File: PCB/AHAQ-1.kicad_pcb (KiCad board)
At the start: 4 copper layers, 50 x 50 mm, 62 parts, among them J1 USB_C_Receptacle_USB2.0_16P, J2 UART, J3 I2C_3, J4 SEN55, J5 I2C_1, J6 I2C_2, J7 I2C_4, J9 E-Paper, Q1 Si1308EDL, U1 ESP32-C6-MINI-1/U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

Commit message: Rename to AHQA-1, README
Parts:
- removed C30, C31: 100nF, Capacitor_SMD:C_0603_1608Metric
- removed J6: I2C_2, Connector_JST:JST_SH_BM04B-SRSS-TB_1x04-1MP_P1.00mm_Vertical
- removed J7: I2C_4, Connector_JST:JST_SH_BM04B-SRSS-TB_1x04-1MP_P1.00mm_Vertical
- J2: footprint Connector_JST:JST_SH_BM03B-SRSS-TB_1x03-1MP_P1.00mm_Vertical -> Connector_JST:JST_SH_SM03B-SRSS-TB_1x03-1MP_P1.00mm_Horizontal
- J3: value I2C_3 -> I2C_1; footprint Connector_JST:JST_SH_BM04B-SRSS-TB_1x04-1MP_P1.00mm_Vertical -> Connector_JST:JST_SH_SM04B-SRSS-TB_1x04-1MP_P1.00mm_Horizontal
- J4: renamed from J5; footprint Connector_JST:JST_SH_BM04B-SRSS-TB_1x04-1MP_P1.00mm_Vertical -> Connector_JST:JST_SH_SM04B-SRSS-TB_1x04-1MP_P1.00mm_Horizontal
- moved J3 12.2 mm to (91.5, 81.5)
- moved J4 8.83 mm to (91.5, 66.0)
- moved C29 5.30 mm to (89.2, 70.0)
- moved J2 1.10 mm to (89.5, 53.3)
- moved C28 1.00 mm to (89.2, 81.5)
- renumbered J4 to J5
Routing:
- net GND: track 167.9 -> 155.0 mm, vias 127 -> 124
- net UART_TX: track 30.6 -> 26.3 mm
- net UART_RX: track 28.9 -> 24.5 mm
- net +3V3_SEN: track 41.0 -> 38.5 mm, vias 9 -> 7
- net SDA: track 90.9 -> 90.2 mm

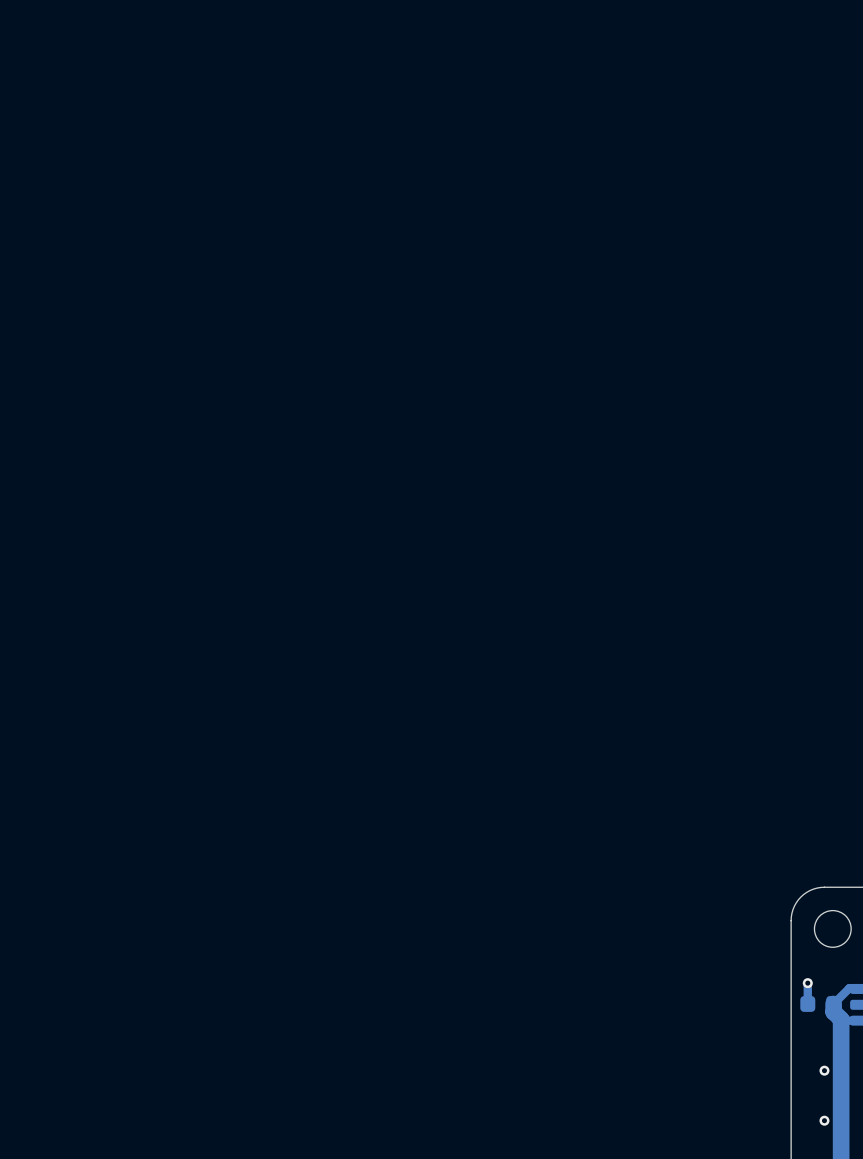
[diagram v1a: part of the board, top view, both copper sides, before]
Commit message: Added FAN output
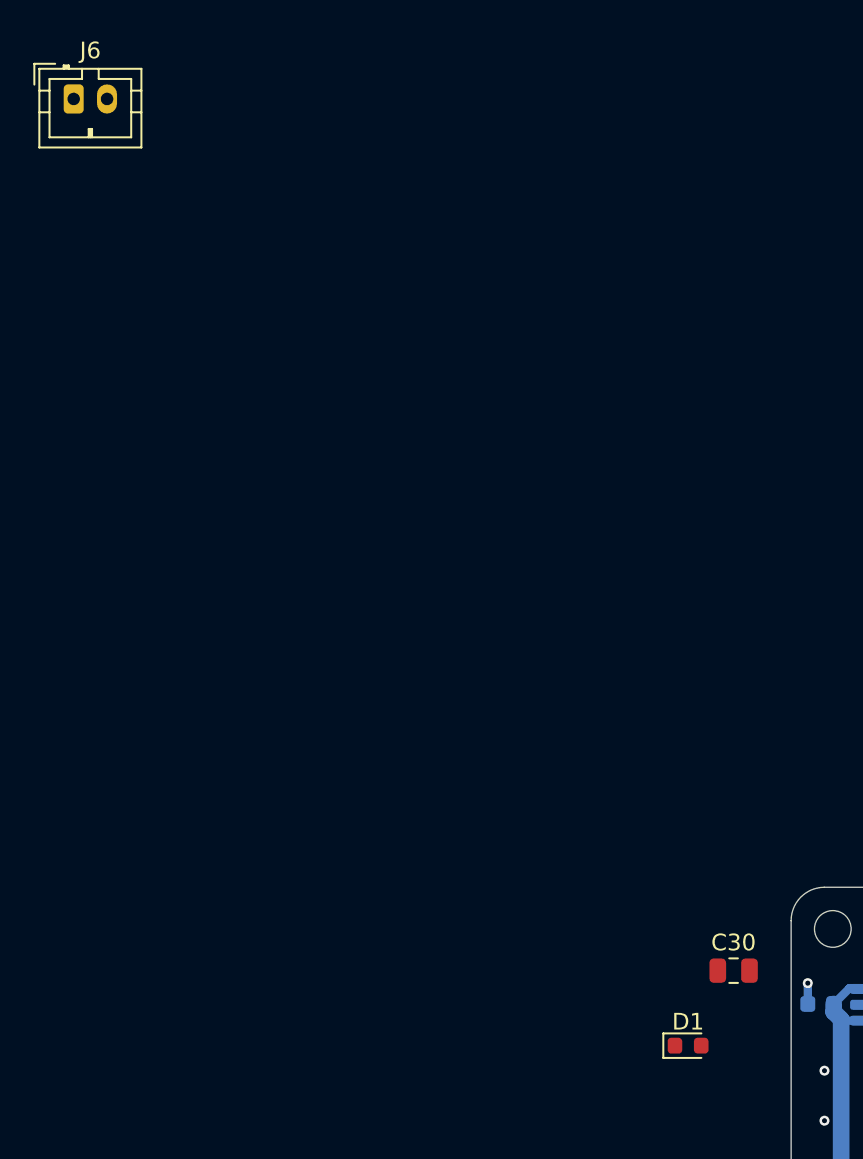
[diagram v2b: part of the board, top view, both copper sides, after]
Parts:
- added C30: 4.7uF, Capacitor_SMD:C_0805_2012Metric, F.Cu at (42.0, 54.5)
- added D1: D, Diode_SMD:D_0603_1608Metric, F.Cu at (39.3, 59.0)
- added J6: FAN, Connector_JST:JST_PH_B2B-PH-K_1x02_P2.00mm_Vertical, F.Cu at (2.48, 2.23)
